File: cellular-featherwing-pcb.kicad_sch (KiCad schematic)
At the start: 16 parts, among them J1 SIM8060-6-0-14-00-A, J2 TSM-116-01-L-SV, J3 TSM-112-01-L-SV, J4 U.FL-R-SMT(10), J5 U.FL-R-SMT(10), U1 BG96, U2 TPS63020DSJR, U3 TXB0108DQSR, U4 MAX8868EUK30+

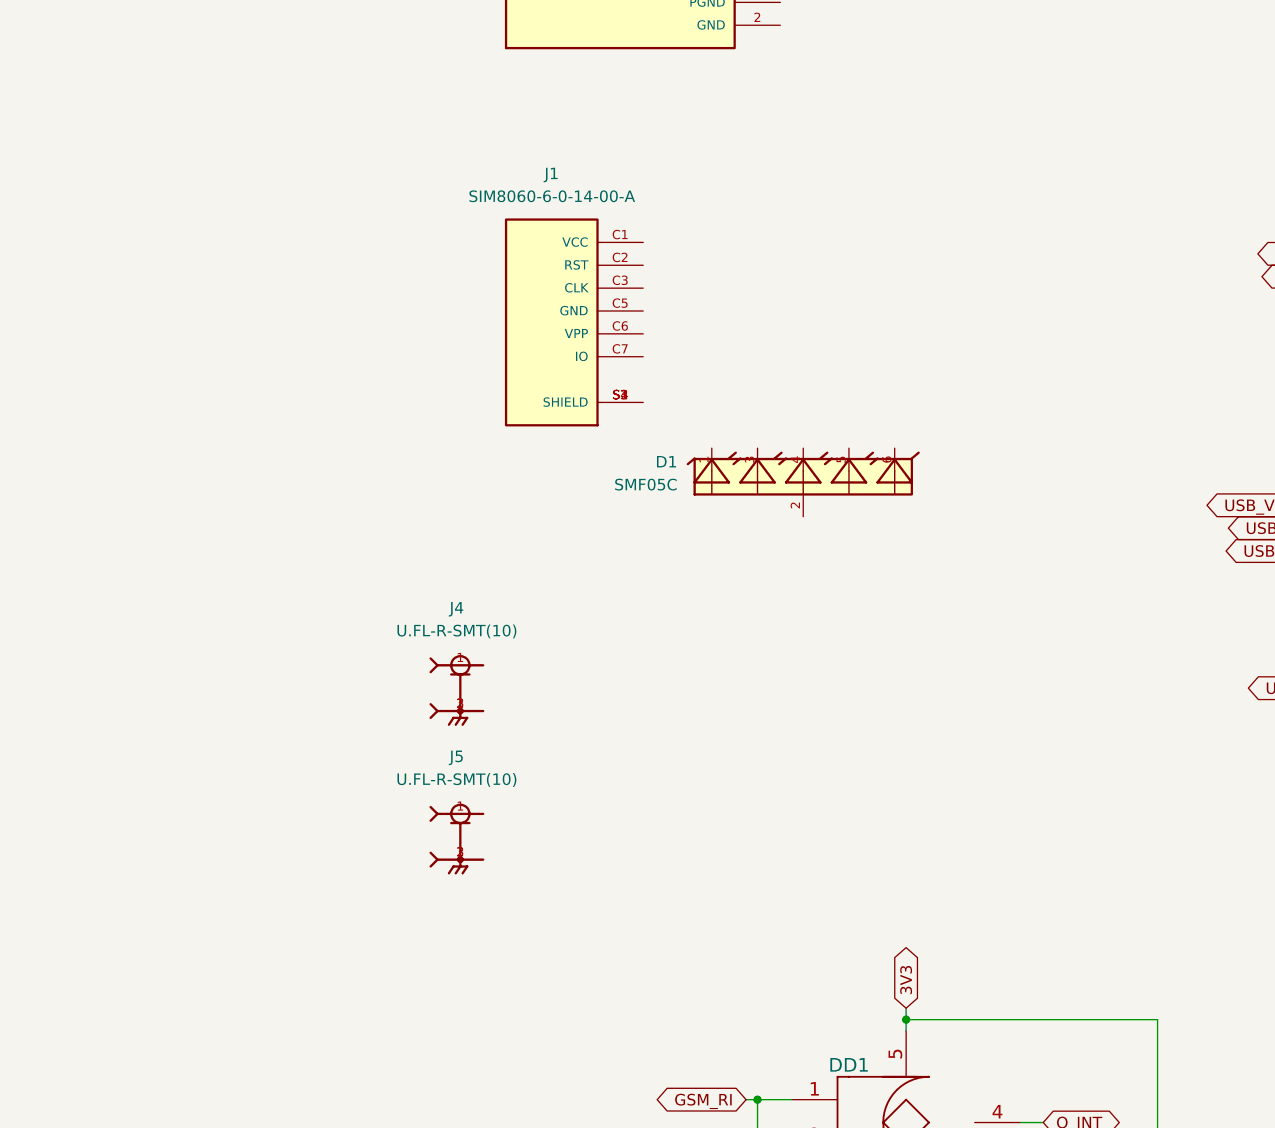
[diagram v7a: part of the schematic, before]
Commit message: Schematic updates for sim card
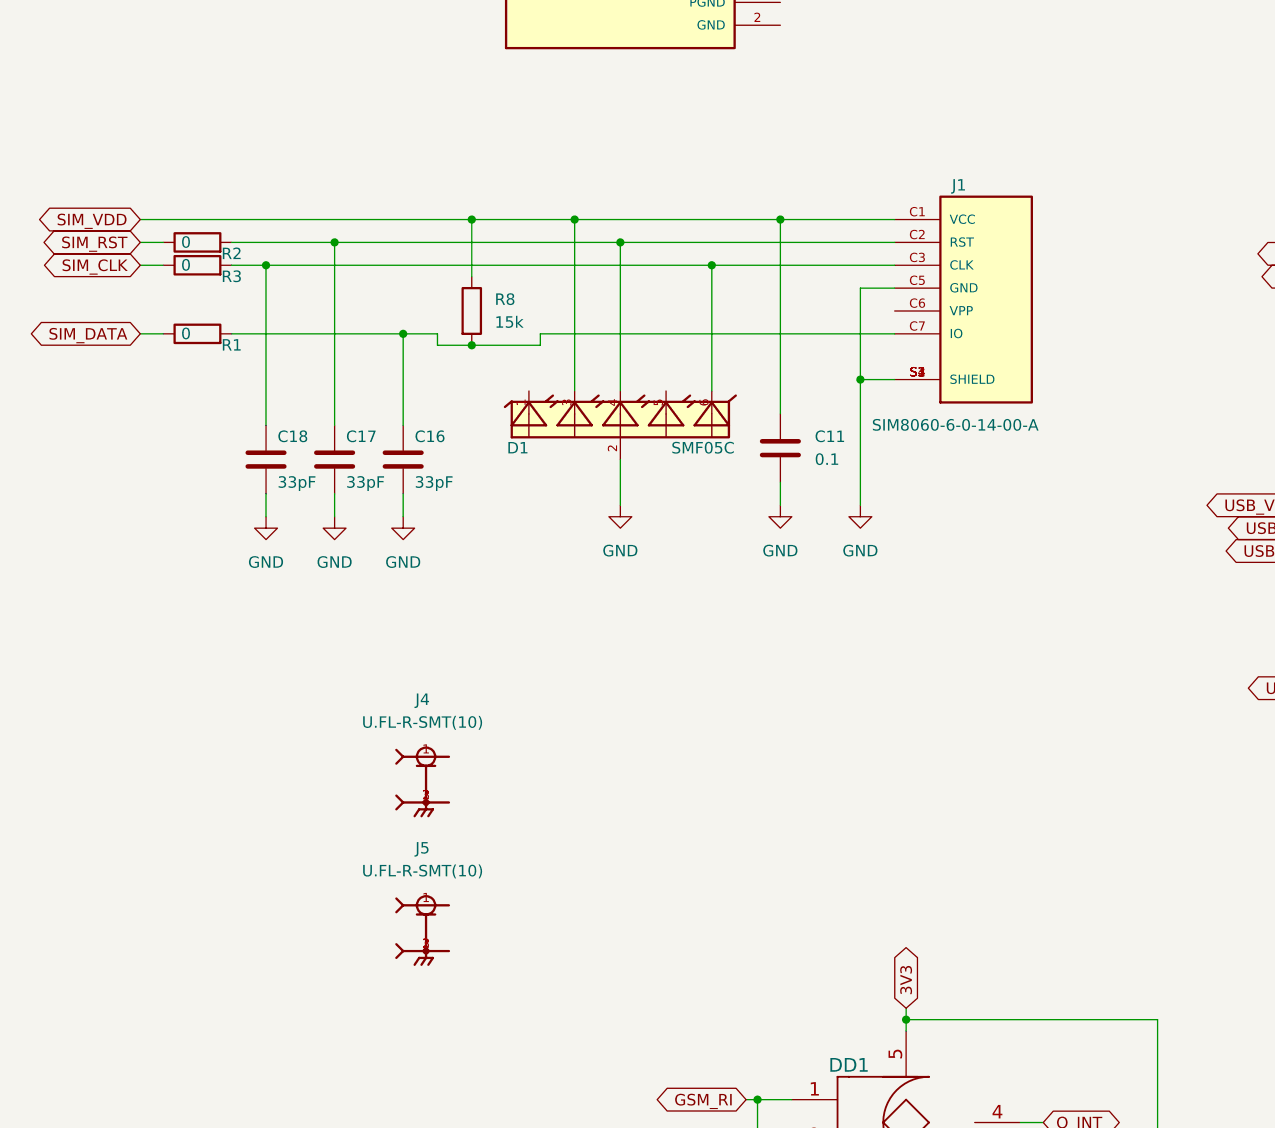
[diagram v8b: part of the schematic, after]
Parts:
- added C11: 0.1, symbol Device:C
- added C16, C17, C18: 33pF, symbol Device:C
- added R1, R2, R3: 0, symbol Device:R
- added R8: 15k, symbol Device:R
- D1: MPN (none) -> SMF05C.TCT
- J1: MP SIM8060-6-0-14-00-A -> (none); MPN (none) -> SIM8060-6-0-14-00-A
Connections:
- net GND: now also D1.2, J1.C5 (GND), J1.S1 (SHIELD), J1.S2 (SHIELD), J1.S3 (SHIELD), J1.S4 (SHIELD), C11.2, C16.2, C17.2, C18.2
- net SIM_CLK: now also R3.1
- net SIM_DATA: now also R1.1
- net SIM_RST: now also R2.1
- net SIM_VDD: now also D1.3, J1.C1 (VCC), C11.1, R8.1
- net at J1.C2 (RST): now also D1.4, C17.1, R2.2
- net at J1.C3 (CLK): now also D1.6, C18.1, R3.2
- net at J1.C7 (IO): now also C16.1, R1.2, R8.2
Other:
- moved on the sheet: D1, J1, J4, J5
